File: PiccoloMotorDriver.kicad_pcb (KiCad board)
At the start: 4 copper layers, 50 x 50 mm, 127 parts, among them J1 01x03_MotorTerminal, J10 Conn_02x09_Odd_Even, J14 Conn_02x09_Odd_Even, J2 Conn_01x05_SWD, J3 Screw_Terminal_01x02_CAN, J4 Screw_Terminal_01x02_RS485, J5 Screw_Terminal_01x02_POWER, J6 Connector, USB-TYPE-C-16P, J7 EXT_AN, J8 Q_ENCODER, J9 Conn_01x03, U1 SP485EEN, U2 XC6210B332MR, U3 XL1509, U4 TJA1050T/CM,118, U5 AS5047D, U6 USBLC6-2SC6, U7 STM32H723VGHx, U8 DRV8316RRGFR, X2 X322516MLB4SI

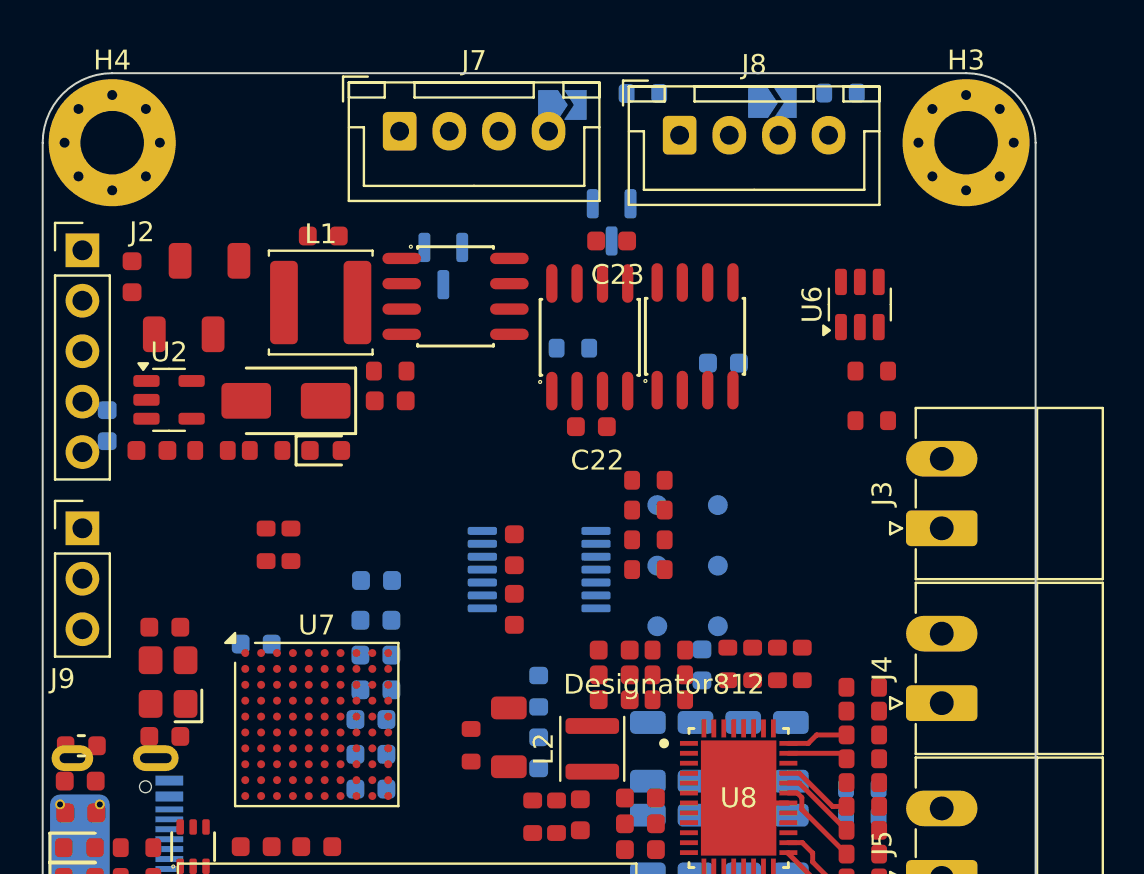
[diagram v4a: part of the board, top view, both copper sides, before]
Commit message: updated mcu connections
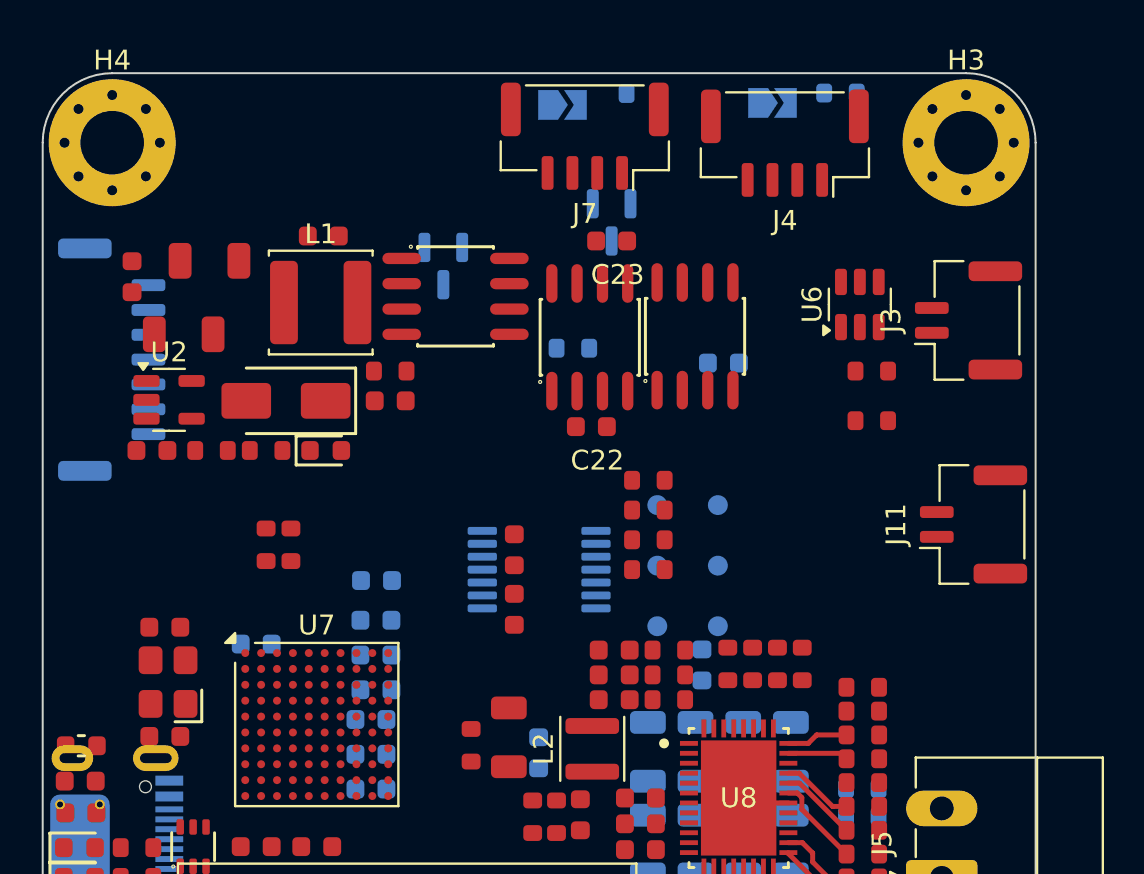
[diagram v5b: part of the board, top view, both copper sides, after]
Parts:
- removed C19: 100nF, PCM_JLCPCB:C_0603
- removed FB1: ~, PCM_JLCPCB:FB_0603
- removed J8: Q_ENCODER, Connector_JST:JST_XH_B4B-XH-A_1x04_P2.50mm_Vertical
- removed J9: Conn_01x03, Connector_PinHeader_2.54mm:PinHeader_1x03_P2.54mm_Vertical
- added J11: CAN, Connector_JST:JST_GH_SM02B-GHS-TB_1x02-1MP_P1.25mm_Horizontal, F.Cu at (160.7, 98.7)
- J10: value Conn_02x09_Odd_Even -> AUX1
- J14: value Conn_02x09_Odd_Even -> AUX0
- J2: value Conn_01x05_SWD -> Debug; footprint Connector_PinHeader_2.54mm:PinHeader_1x05_P2.54mm_Vertical -> Connector_JST:JST_GH_SM07B-GHS-TB_1x07-1MP_P1.25mm_Horizontal; moved to B.Cu
- J3: value Screw_Terminal_01x02_CAN -> RS485; footprint Connector_Phoenix_MC:PhoenixContact_MC_1,5_2-G-3.5_1x02_P3.50mm_Horizontal -> Connector_JST:JST_GH_SM02B-GHS-TB_1x02-1MP_P1.25mm_Horizontal
- J4: value Screw_Terminal_01x02_RS485 -> Conn_01x05; footprint Connector_Phoenix_MC:PhoenixContact_MC_1,5_2-G-3.5_1x02_P3.50mm_Horizontal -> Connector_JST:JST_GH_SM04B-GHS-TB_1x04-1MP_P1.25mm_Horizontal
- J7: value EXT_AN -> Conn_01x05; footprint Connector_JST:JST_XH_B4B-XH-A_1x04_P2.50mm_Vertical -> Connector_JST:JST_GH_SM04B-GHS-TB_1x04-1MP_P1.25mm_Horizontal
- moved J4 29.3 mm to (151.2, 79.5), turned to 180 degrees
- moved J3 10.6 mm to (160.4, 88.4)
- moved J7 9.33 mm to (141.1, 79.2), turned to 180 degrees
- moved J2 5.70 mm to (117.3, 90.4), turned to 90 degrees
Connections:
- C12 pad 1: Net-(U8-AVDD) -> +3.3V
- J10 pad 1: unconnected-(J10-Pin_1-Pad1) -> /Mcu/PB13
- J10 pad 10: unconnected-(J10-Pin_10-Pad10) -> /Mcu/PD12
- J10 pad 11: unconnected-(J10-Pin_11-Pad11) -> /Mcu/PA5
- J10 pad 12: unconnected-(J10-Pin_12-Pad12) -> /Mcu/PD13
- J10 pad 13: unconnected-(J10-Pin_13-Pad13) -> /Mcu/PC13
- J10 pad 14: unconnected-(J10-Pin_14-Pad14) -> /Mcu/PD14
- J10 pad 15: unconnected-(J10-Pin_15-Pad15) -> /Mcu/PC14
- J10 pad 16: unconnected-(J10-Pin_16-Pad16) -> /Mcu/PD15
- J10 pad 17: unconnected-(J10-Pin_17-Pad17) -> /Mcu/PC15
- J10 pad 18: unconnected-(J10-Pin_18-Pad18) -> /Mcu/PB12
- J10 pad 2: unconnected-(J10-Pin_2-Pad2) -> /Mcu/PD8
- J10 pad 3: unconnected-(J10-Pin_3-Pad3) -> /Mcu/PB14
- J10 pad 4: unconnected-(J10-Pin_4-Pad4) -> /Mcu/PD9
- J10 pad 5: unconnected-(J10-Pin_5-Pad5) -> /Mcu/PC4
- J10 pad 6: unconnected-(J10-Pin_6-Pad6) -> /Mcu/PD10
- J10 pad 7: unconnected-(J10-Pin_7-Pad7) -> /Mcu/PC5
- J10 pad 8: unconnected-(J10-Pin_8-Pad8) -> /Mcu/PD11
- J10 pad 9: unconnected-(J10-Pin_9-Pad9) -> /Mcu/PA8
- J14 pad 1: unconnected-(J14-Pin_1-Pad1) -> /Mcu/PE0
- J14 pad 10: unconnected-(J14-Pin_10-Pad10) -> /Mcu/PD0
- J14 pad 11: unconnected-(J14-Pin_11-Pad11) -> /Mcu/PE5
- J14 pad 12: unconnected-(J14-Pin_12-Pad12) -> /Mcu/PD4
- J14 pad 13: unconnected-(J14-Pin_13-Pad13) -> /Mcu/PE6
- J14 pad 14: unconnected-(J14-Pin_14-Pad14) -> /Mcu/PD5
- J14 pad 15: unconnected-(J14-Pin_15-Pad15) -> /Mcu/PE7
- J14 pad 16: unconnected-(J14-Pin_16-Pad16) -> /Mcu/PD6
- J14 pad 17: unconnected-(J14-Pin_17-Pad17) -> /Mcu/PE11
- J14 pad 18: unconnected-(J14-Pin_18-Pad18) -> /Mcu/PD7
- J14 pad 2: unconnected-(J14-Pin_2-Pad2) -> /Mcu/PE12
- J14 pad 3: unconnected-(J14-Pin_3-Pad3) -> /Mcu/PE1
- J14 pad 4: unconnected-(J14-Pin_4-Pad4) -> /Mcu/PE13
- J14 pad 5: unconnected-(J14-Pin_5-Pad5) -> /Mcu/PE2
- J14 pad 6: unconnected-(J14-Pin_6-Pad6) -> /Mcu/PE14
- J14 pad 7: unconnected-(J14-Pin_7-Pad7) -> /Mcu/PE3
- J14 pad 8: unconnected-(J14-Pin_8-Pad8) -> /Mcu/PE15
- J14 pad 9: unconnected-(J14-Pin_9-Pad9) -> /Mcu/PE4
- J3 pad 1: /IO/CAN+ -> /IO/RS485-
- J3 pad 2: /IO/CAN- -> /IO/RS485+
- J4 pad 1: /IO/RS485- -> GND
- J4 pad 2: /IO/RS485+ -> GND
- J7 pad 2: +3.3V -> GND
- J7 pad 3: Net-(J7-Pin_3) -> +3.3V
- R30 pad 1: Net-(J8-Pin_3) -> Net-(J4-Pin_4)
- R33 pad 1: Net-(J7-Pin_4) -> Net-(J7-Pin_5)
- R36 pad 1: Net-(J7-Pin_3) -> Net-(J7-Pin_4)
- U7 pad A1: unconnected-(U7-PC14-PadA1) -> /Mcu/PC14
- U7 pad A2: unconnected-(U7-PC13-PadA2) -> /Mcu/PC13
- U7 pad A4: CAN_TX -> DRV_SPI_~{SCS}
- U7 pad A5: unconnected-(U7-PB7-PadA5) -> /Mcu/PB7
- U7 pad A8: unconnected-(U7-PA15(JTDI)-PadA8) -> RS485_DE
- U7 pad B1: unconnected-(U7-PC15-PadB1) -> /Mcu/PC15
- U7 pad B3: unconnected-(U7-PE3-PadB3) -> /Mcu/PE3
- U7 pad B5: unconnected-(U7-PB6-PadB5) -> /Mcu/PB6
- U7 pad B6: unconnected-(U7-PD5-PadB6) -> /Mcu/PD5
- U7 pad C3: unconnected-(U7-PE4-PadC3) -> /Mcu/PE4
- U7 pad C6: unconnected-(U7-PD6-PadC6) -> /Mcu/PD6
- U7 pad C8: unconnected-(U7-PC12-PadC8) -> DEBUG_RX
- U7 pad D3: unconnected-(U7-PE5-PadD3) -> /Mcu/PE5
- U7 pad D6: unconnected-(U7-PD7-PadD6) -> /Mcu/PD7
- U7 pad D7: unconnected-(U7-PD4-PadD7) -> /Mcu/PD4
- U7 pad D8: unconnected-(U7-PD0-PadD8) -> /Mcu/PD0
- U7 pad D9: unconnected-(U7-PA8-PadD9) -> /Mcu/PA8
- U7 pad E10: QUAD_ENC_B -> UI_LED_RED
- U7 pad E3: unconnected-(U7-PE6-PadE3) -> /Mcu/PE6
- U7 pad E8: unconnected-(U7-PD1-PadE8) -> CAN_TX
- U7 pad E9: unconnected-(U7-PC9-PadE9) -> DRV_OFF
- U7 pad F10: QUAD_ENC_A -> UI_LED_YELLOW
- U7 pad F2: DRV_SPI_SDI -> DRV_AN_REF
- U7 pad F3: AN_DRV_SO_C -> DRV_SPI_SDI
- U7 pad F9: DRV_OFF -> UI_LED_BLUE
- U7 pad G2: UI_LED_RED -> QUAD_ENC_A
- U7 pad G4: AN_DRV_SO_B -> /Mcu/PC4
- U7 pad G7: unconnected-(U7-PE14-PadG7) -> /Mcu/PE14
- U7 pad G8: unconnected-(U7-PD15-PadG8) -> /Mcu/PD15
- U7 pad G9: unconnected-(U7-PD11-PadG9) -> /Mcu/PD11
- U7 pad H10: unconnected-(U7-PB14-PadH10) -> /Mcu/PB14
- U7 pad H2: UI_LED_YELLOW -> QUAD_ENC_B
- U7 pad H3: unconnected-(U7-PA5-PadH3) -> /Mcu/PA5
- U7 pad H4: AN_VBUS -> /Mcu/PC5
- U7 pad H5: unconnected-(U7-PE7-PadH5) -> /Mcu/PE7
- U7 pad H6: unconnected-(U7-PE11-PadH6) -> /Mcu/PE11
- U7 pad H7: unconnected-(U7-PE15-PadH7) -> /Mcu/PE15
- U7 pad H8: unconnected-(U7-PD14-PadH8) -> /Mcu/PD14
- U7 pad H9: unconnected-(U7-PD10-PadH9) -> /Mcu/PD10
- U7 pad J10: unconnected-(U7-PD13-PadJ10) -> /Mcu/PD13
- U7 pad J2: UI_LED_BLUE -> AN_VBUS
- U7 pad J4: AN_EXT_IN_0 -> ~{DRV_FAULT}
- U7 pad J6: unconnected-(U7-PE12-PadJ6) -> /Mcu/PE12
- U7 pad J7: unconnected-(U7-PB10-PadJ7) -> /Mcu/PB10
- U7 pad J8: unconnected-(U7-PB13-PadJ8) -> /Mcu/PB13
- U7 pad J9: unconnected-(U7-PD9-PadJ9) -> /Mcu/PD9
- U7 pad K10: unconnected-(U7-PD12-PadK10) -> /Mcu/PD12
- U7 pad K2: RS485_DE -> AN_EXT_IN_0
- U7 pad K3: DRV_AN_REF -> AN_DRV_SO_B
- U7 pad K4: ~{DRV_FAULT} -> AN_DRV_SO_C
- U7 pad K6: unconnected-(U7-PE13-PadK6) -> /Mcu/PE13
- U7 pad K7: unconnected-(U7-PB11-PadK7) -> /Mcu/PB11
- U7 pad K8: DRV_SPI_~{SCS} -> /Mcu/PB12
- U7 pad K9: unconnected-(U7-PD8-PadK9) -> /Mcu/PD8
- U8 pad 25: Net-(U8-AVDD) -> +3.3V

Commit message: layout placement
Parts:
- removed J10: AUX1, Connector_PinHeader_2.54mm:PinHeader_2x09_P2.54mm_Vertical
- removed J14: AUX0, Connector_PinHeader_2.54mm:PinHeader_2x09_P2.54mm_Vertical
- added J8: AUX0, Connector_PinSocket_2.54mm:PinSocket_2x10_P2.54mm_Vertical, F.Cu at (117.6, 84.2)
- added J9: AUX0, Connector_PinSocket_2.54mm:PinSocket_2x10_P2.54mm_Vertical, F.Cu at (144.8, 123.0)
- C1, C2, R25, R26: moved to B.Cu
- J6, R1, R15: moved to F.Cu
- moved TP5 45.4 mm to (188.5, 116.0)
- moved J6 45.4 mm to (163.0, 112.0)
- moved TP6 44.4 mm to (189.0, 120.5)
- moved TP3 42.1 mm to (186.5, 106.5)
- moved J1 41.8 mm to (152.9, 79.8), turned to 180 degrees
- moved D4 39.4 mm to (154.0, 124.0), turned to 180 degrees
- moved D6 38.8 mm to (154.0, 122.4), turned to 180 degrees
- moved D7 38.4 mm to (154.0, 120.8), turned to 180 degrees
- moved TP1 38.4 mm to (181.0, 110.5)
- moved TP4 38.3 mm to (181.5, 119.0)
- moved TP2 38.1 mm to (181.5, 115.5)
- moved R22 37.1 mm to (113.1, 56.4)
- moved JP2 37.1 mm to (109.1, 57.0)
- moved R8 37.1 mm to (123.1, 56.4)
- moved JP1 37.1 mm to (119.6, 56.9)
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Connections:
- J11 pad MP: GND -> (no net)
- J4 pad 1: GND -> Net-(J4-Pin_1)
- J4 pad 2: GND -> Net-(J4-Pin_2)
- J4 pad 4: Net-(J4-Pin_4) -> GND
- J7 pad 1: GND -> Net-(J7-Pin_1)
- J7 pad 2: GND -> Net-(J7-Pin_2)
- J7 pad 4: Net-(J7-Pin_4) -> GND
- R30 pad 1: Net-(J4-Pin_4) -> Net-(J4-Pin_2)
- R33 pad 1: Net-(J7-Pin_5) -> Net-(J7-Pin_1)
- R35 pad 1: Net-(J4-Pin_5) -> Net-(J4-Pin_1)
- R36 pad 1: Net-(J7-Pin_4) -> Net-(J7-Pin_2)
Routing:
- net Net-(J1-Pin_3): track 0.00 -> 12.6 mm
- net Net-(J1-Pin_1): track 0.00 -> 11.7 mm
- net Net-(J1-Pin_2): track 0.00 -> 11.0 mm
- net Net-(U8-SCLK): track 0.00 -> 9.26 mm
- net Vdrive: track 0.00 -> 8.57 mm
- net Net-(U8-SOA): track 0.00 -> 8.46 mm
- net Net-(U8-SOB): track 0.00 -> 7.31 mm
- net Net-(U8-SDO): track 0.00 -> 7.08 mm
- net Net-(U8-SCS_N): track 0.00 -> 6.87 mm
- net Net-(U8-SOC): track 0.00 -> 6.09 mm
- net Net-(U8-SDI): track 0.00 -> 5.53 mm
- net Net-(U8-INLB): track 0.00 -> 3.79 mm
- net Net-(U8-SLEEP_N): track 0.00 -> 3.67 mm
- net Net-(U8-INHC): track 3.04 -> 6.47 mm
- net Net-(U8-INHB): track 3.62 -> 6.72 mm
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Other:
- board size 50 x 50 mm -> 55 x 50 mm

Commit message: more layout
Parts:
- removed C10: 10uF, PCM_JLCPCB:C_1206
- removed L2: 47uH, 200mA (JLC-C83420), Inductor_SMD:L_Changjiang_FNR3010S
- removed R34: 0Ω, PCM_JLCPCB:R_0603
- added FID1: Fiducial, Fiducial:Fiducial_0.5mm_Mask1mm, F.Cu at (114.0, 117.8)
- added FID2: Fiducial, Fiducial:Fiducial_0.5mm_Mask1mm, F.Cu at (162.2, 118.0)
- added FID3: Fiducial, Fiducial:Fiducial_0.5mm_Mask1mm, F.Cu at (120.0, 76.0)
- added TP7: GND_BK, TestPoint:TestPoint_Pad_D1.0mm, B.Cu at (155.9, 90.7)
- added TP8: FB_BK, TestPoint:TestPoint_Pad_D1.0mm, B.Cu at (157.7, 91.7)
- added TP9: SW_BK, TestPoint:TestPoint_Pad_D1.0mm, B.Cu at (157.7, 89.7)
- C17, C28, C29, FB2: moved to B.Cu
- C21, R21, TP1, TP2, TP3, TP4, TP5, TP6: moved to F.Cu
- moved JP2 70.9 mm to (165.5, 100.0), turned to 180 degrees
- moved R22 65.9 mm to (162.4, 100.2), turned to 180 degrees
- moved U3 62.8 mm to (149.0, 113.6), turned to 180 degrees
- moved JP1 58.0 mm to (165.5, 92.4), turned to 180 degrees
- moved C23 57.4 mm to (157.8, 106.4)
- moved TP6 53.8 mm to (138.6, 101.6)
- moved R8 53.4 mm to (162.5, 92.4), turned to 180 degrees
- moved D8 53.1 mm to (165.2, 95.4), turned to 180 degrees
- moved TP5 49.9 mm to (140.4, 102.6)
- moved TP2 46.5 mm to (138.6, 97.6)
- moved TP3 46.5 mm to (140.4, 100.6)
- moved TP4 45.9 mm to (140.4, 98.6)
- moved D9 43.9 mm to (165.2, 103.0), turned to 180 degrees
- moved TP1 43.8 mm to (138.6, 99.6)
- moved C21 35.5 mm to (154.8, 98.4), turned to 0 degrees
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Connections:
- D1 pad 4: QUAD_ENC_B -> QUAD_ENC_A
- D1 pad 6: QUAD_ENC_A -> QUAD_ENC_B
- D5 pad 1: Net-(D5-Pad1) -> GND
- D5 pad 2: +3.3V -> Net-(D5-Pad2)
- R3 pad 1: Net-(D5-Pad1) -> +3.3V
- R3 pad 2: GND -> Net-(D5-Pad2)
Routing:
- net +5V: track 0.00 -> 55.3 mm, vias 0 -> 3
- net AN_EXT_IN_0: track 0.00 -> 45.5 mm
- net Vdrive: track 8.57 -> 49.0 mm, vias 0 -> 21
- net /Mcu/PD5: track 0.00 -> 36.8 mm, vias 0 -> 1
- net /Mcu/PD4: track 0.00 -> 33.5 mm, vias 0 -> 1
- net /Mcu/PE12: track 0.00 -> 30.8 mm, vias 0 -> 3
- net /Mcu/PD6: track 0.00 -> 28.9 mm, vias 0 -> 1
- net /Mcu/PE13: track 0.00 -> 28.6 mm, vias 0 -> 3
- net AN_EXT_IN_1: track 0.00 -> 27.3 mm, vias 0 -> 2
- net GND: track 4.73 -> 31.6 mm, vias 3 -> 50
- net /Mcu/PD7: track 0.00 -> 26.8 mm, vias 0 -> 2
- net /Mcu/PE15: track 0.00 -> 25.6 mm, vias 0 -> 3
- net /Mcu/PB11: track 0.00 -> 25.4 mm, vias 0 -> 2
- net ~{DRV_FAULT}: track 0.00 -> 24.9 mm, vias 0 -> 2
- net /Mcu/PB10: track 0.00 -> 24.5 mm, vias 0 -> 2
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- added copper zone on In2.Cu, net +3.3V
- added copper zone on B.Cu, net GND
- added copper zone on F.Cu, net GND
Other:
- board text added: "ANLG"
- board text added: "CAN"
- board text added: "ENC"
- board text added: "RS485"

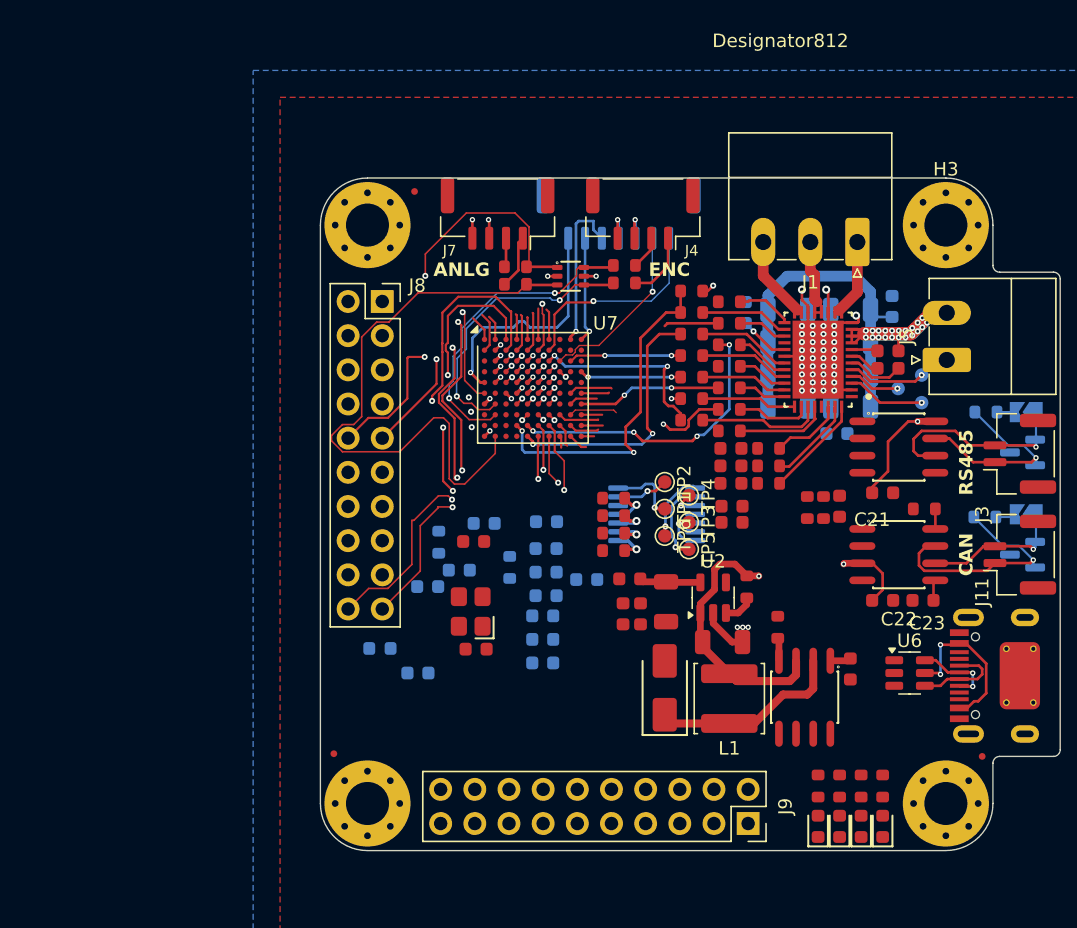
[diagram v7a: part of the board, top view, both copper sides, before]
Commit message: Reroute mcu lines, updated can, motor timer pins
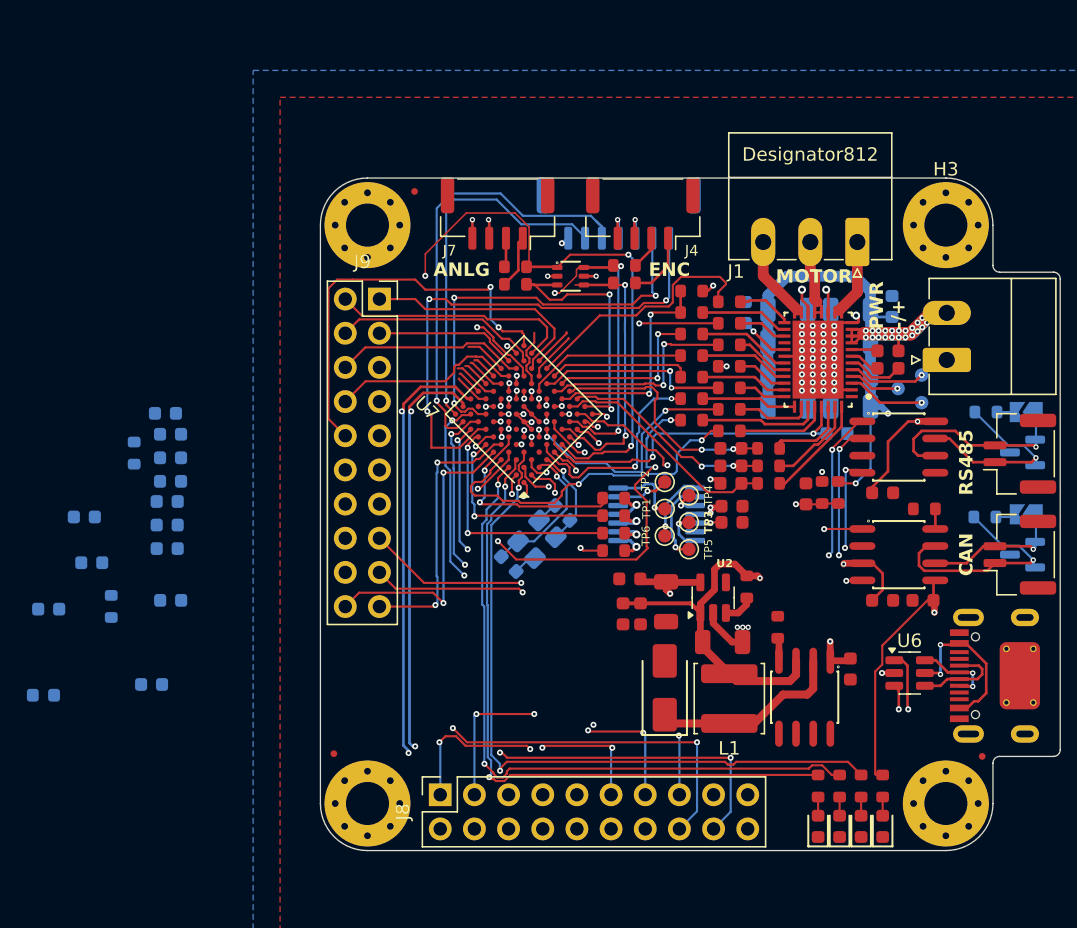
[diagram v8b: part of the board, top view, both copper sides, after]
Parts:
- C8, C9, X2: moved to B.Cu
- moved J9 47.7 mm to (117.4, 84.0), turned to 0 degrees
- moved J8 36.9 mm to (121.9, 120.8), turned to 90 degrees
- moved C3 31.0 mm to (101.9, 106.4)
- moved C2 29.7 mm to (95.5, 100.2)
- moved C36 29.5 mm to (101.5, 92.5)
- moved R25 29.2 mm to (99.2, 95.5)
- moved C30 29.2 mm to (101.9, 95.8)
- moved C31 29.2 mm to (101.6, 100.8)
- moved C32 29.2 mm to (101.6, 99.1)
- moved C33 29.2 mm to (101.9, 97.6)
- moved C34 29.2 mm to (101.9, 94.1)
- moved C35 29.2 mm to (101.6, 102.6)
- moved C1 28.2 mm to (92.8, 107.0)
- moved C29 27.3 mm to (96.0, 103.6)
- moved FB2 25.3 mm to (92.4, 113.5)
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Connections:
- C11 pad 1: AN_DRV_AN_REF -> DRV_AN_REF
- C23 pad 1: +3V3 -> +3.3V
- J8 pad 20: /Mcu/PB11 -> /Mcu/PC9
- J8 pad 5: /Mcu/PE2 -> /Mcu/PC8
- J8 pad 7: /Mcu/PE3 -> /Mcu/PC7
- J8 pad 9: /Mcu/PE4 -> /Mcu/PC6
- U4 pad 5: +3V3 -> +3.3V
- U7 pad A3: /Mcu/PE2 -> UI_LED_BLUE
- U7 pad B3: /Mcu/PE3 -> UI_LED_RED
- U7 pad B4: CAN_RX -> unconnected-(U7-PB8-PadB4)
- U7 pad C3: /Mcu/PE4 -> UI_LED_YELLOW
- U7 pad C9: PWM_B_H -> unconnected-(U7-PA9-PadC9)
- U7 pad D10: PWM_C_H -> unconnected-(U7-PA10-PadD10)
- U7 pad D8: /Mcu/PD0 -> CAN_RX
- U7 pad E10: UI_LED_RED -> /Mcu/PC7
- U7 pad E9: DRV_OFF -> /Mcu/PC9
- U7 pad F10: UI_LED_YELLOW -> /Mcu/PC6
- U7 pad F9: UI_LED_BLUE -> /Mcu/PC8
- U7 pad G10: PWM_C_L -> unconnected-(U7-PB15-PadG10)
- U7 pad H6: /Mcu/PE11 -> PWM_B_H
- U7 pad J6: /Mcu/PE12 -> PWM_C_L
- U7 pad K6: /Mcu/PE13 -> PWM_C_H
- U7 pad K7: /Mcu/PB11 -> DRV_OFF
- U8 pad 37: AN_DRV_AN_REF -> DRV_AN_REF
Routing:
- net USB-: track 0.00 -> 76.9 mm, vias 0 -> 3
- net USB+: track 0.00 -> 71.7 mm, vias 0 -> 3
- net RS485_DI: track 0.00 -> 51.4 mm, vias 0 -> 4
- net RS485_RO: track 0.00 -> 51.2 mm, vias 0 -> 4
- net UI_LED_YELLOW: track 2.07 -> 52.9 mm, vias 0 -> 2
- net UI_LED_RED: track 0.00 -> 49.4 mm, vias 0 -> 2
- net RS485_DE: track 0.00 -> 48.5 mm, vias 0 -> 4
- net UI_LED_BLUE: track 3.24 -> 50.6 mm, vias 0 -> 2
- net +3.3V: track 17.7 -> 61.6 mm, vias 11 -> 9
- net CAN_RX: track 2.82 -> 45.0 mm, vias 0 -> 2
- net CAN_TX: track 0.00 -> 40.7 mm, vias 0 -> 2
- net /Mcu/PD5: track 36.8 -> 1.61 mm
- net Vdrive: track 49.0 -> 83.3 mm, vias 21 -> 24
- net /Mcu/PD4: track 33.5 -> 0.56 mm
- net /Mcu/PE12: track 30.8 -> 0.00 mm, vias 3 -> 0
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- added copper zone on In4.Cu, net +3.3V
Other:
- copper layers 4 -> 6
- board text added: "MOTOR"
- board text added: "PWR -/+"
